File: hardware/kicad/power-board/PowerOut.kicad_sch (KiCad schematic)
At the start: 17 parts, among them J1 3.3V LoRaWAN, J2 3.3V SWARM, J3 Conn_01x02, J4 5V, J6 12V

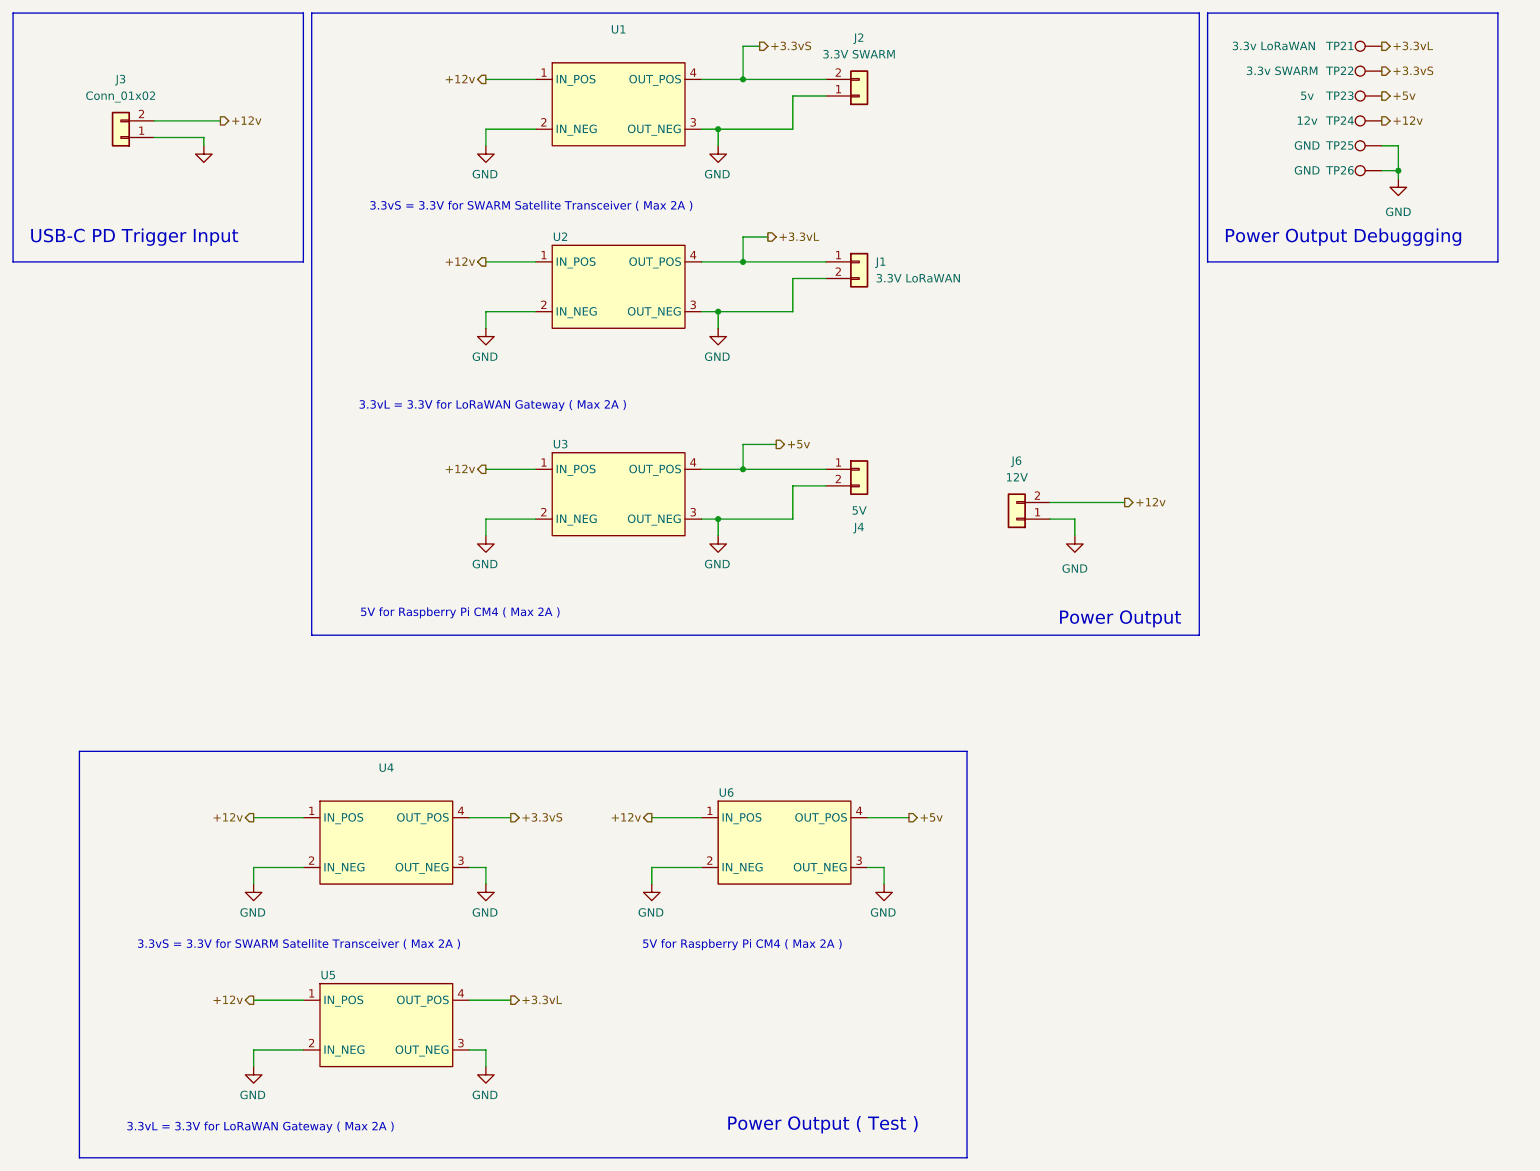
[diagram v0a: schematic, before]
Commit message: fix power polarity in power board test
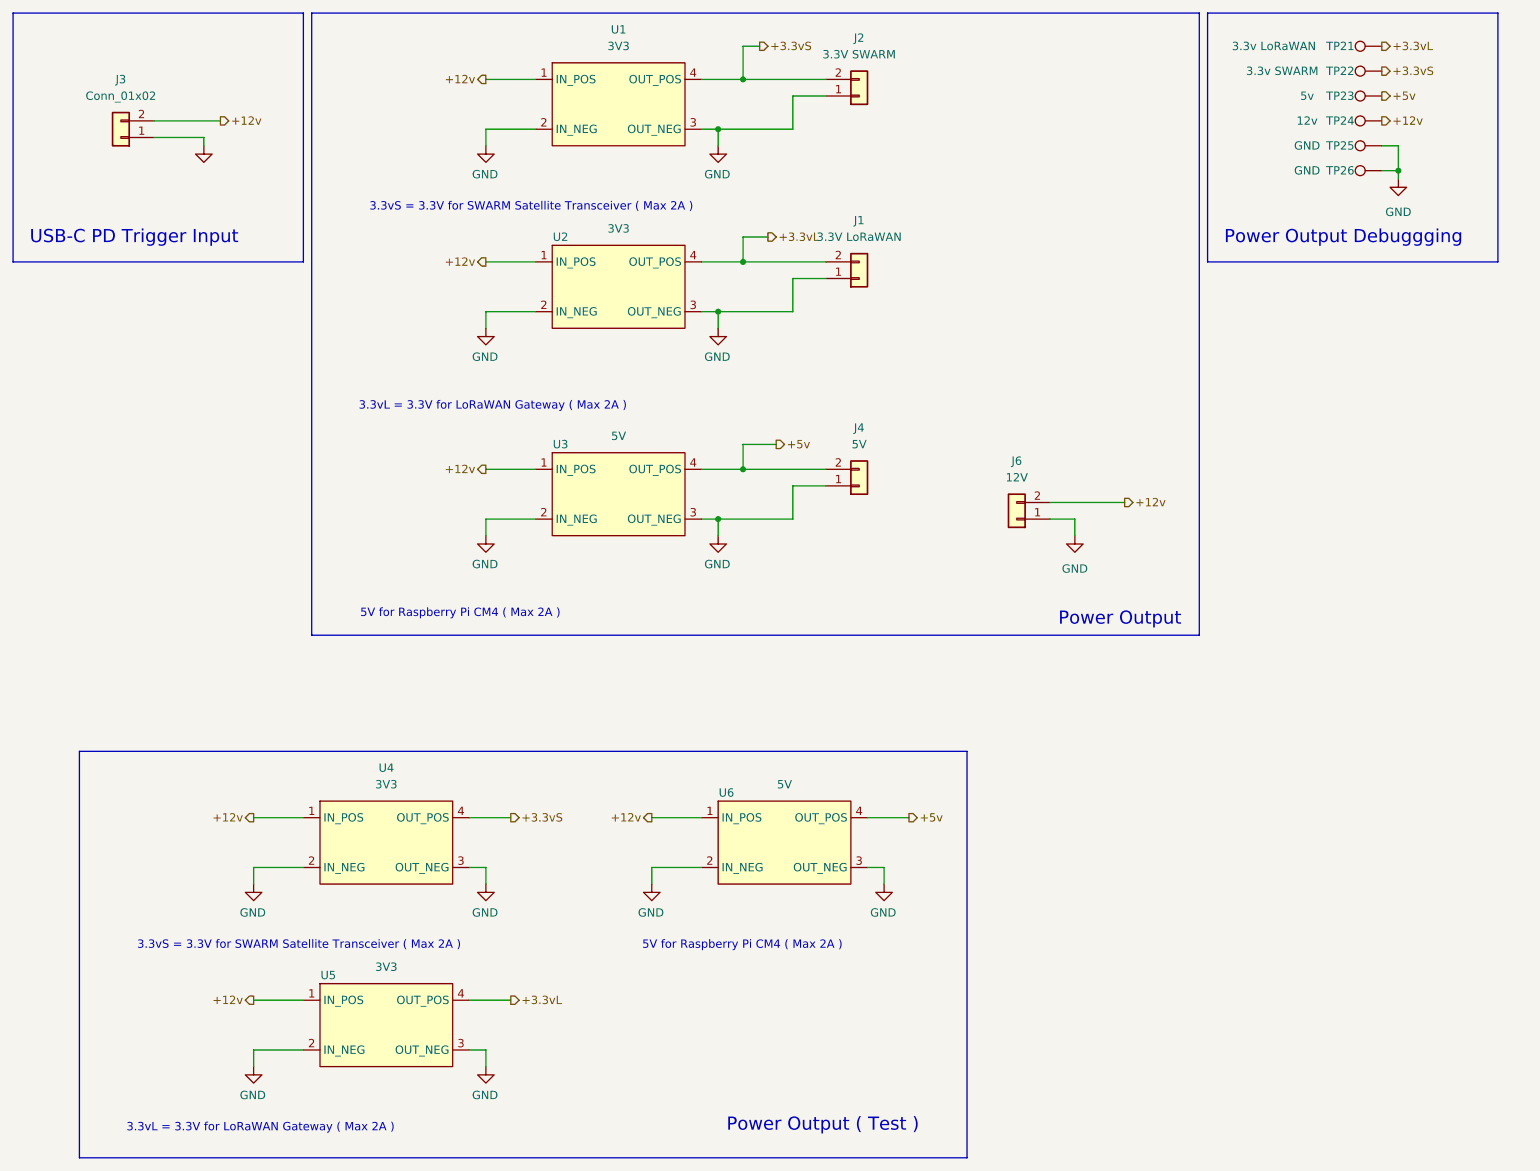
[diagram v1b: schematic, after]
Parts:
- U1, U2: value (none) -> 3V3; footprint (none) -> Teapot:LM2596Module
- U3: value (none) -> 5V; footprint (none) -> Teapot:LM2596Module
- U4, U5: value (none) -> 3V3; footprint (none) -> Teapot:MiniMP1584ENModule
- U6: value (none) -> 5V; footprint (none) -> Teapot:MiniMP1584ENModule
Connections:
- net +3.3vL: now also J1.2 (Pin_2); no longer J1.1 (Pin_1)
- net +5v: now also J4.2 (Pin_2); no longer J4.1 (Pin_1)
- net GND: now also J1.1 (Pin_1), J4.1 (Pin_1); no longer J1.2 (Pin_2), J4.2 (Pin_2)
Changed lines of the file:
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@@
     (pin "1")
   )
-  (symbol (lib_id "Connector_Generic:Conn_01x02") (at 144.78 85.09 0) (unit 1)
-    (in_bom yes) (on_board yes)
-    (property "Reference" "J4" (id 0) (at 144.78 93.98 0))
-    (property "Value" "5V" (id 1) (at 144.78 91.44 0))
-    (property "Footprint" "Connector_Wire:SolderWire-0.5sqmm_1x02_P4.8mm_D0.9mm_OD2.3mm" (id 2) (at 144.78 85.09 0)
-      (effects (font (size 1.27 1.27)) hide)
-    )
-    (property "Datasheet" "~" (id 3) (at 144.78 85.09 0)
+  (symbol (lib_id "Connector_Generic:Conn_01x02") (at 144.78 87.63 0) (mirror x) (unit 1)
+    (in_bom yes) (on_board yes)
+    (property "Reference" "J4" (id 0) (at 144.78 78.74 0))
+    (property "Value" "5V" (id 1) (at 144.78 81.28 0))
+    (property "Footprint" "Connector_Wire:SolderWire-0.5sqmm_1x02_P4.8mm_D0.9mm_OD2.3mm" (id 2) (at 144.78 87.63 0)
+      (effects (font (size 1.27 1.27)) hide)
+    )
+    (property "Datasheet" "~" (id 3) (at 144.78 87.63 0)
       (effects (font (size 1.27 1.27)) hide)
     )
@@
     (in_bom yes) (on_board yes)
     (property "Reference" "U6" (id 0) (at 124.46 134.62 0))
-    (property "Value" "" (id 1) (at 133.35 133.35 0))
-    (property "Footprint" "" (id 2) (at 133.35 133.985 0)
+    (property "Value" "5V" (id 1) (at 133.35 133.35 0))
+    (property "Footprint" "Teapot:MiniMP1584ENModule" (id 2) (at 133.35 133.985 0)
       (effects (font (size 1.27 1.27)) hide)
     )
@@
     (in_bom yes) (on_board yes) (fields_autoplaced)
     (property "Reference" "U1" (id 0) (at 107.95 17.78 0))
-    (property "Value" "" (id 1) (at 107.95 20.32 0))
-    (property "Footprint" "" (id 2) (at 107.95 20.955 0)
+    (property "Value" "3V3" (id 1) (at 107.95 20.32 0))
+    (property "Footprint" "Teapot:LM2596Module" (id 2) (at 107.95 20.955 0)
       (effects (font (size 1.27 1.27)) hide)
     )
@@
     (in_bom yes) (on_board yes) (fields_autoplaced)
     (property "Reference" "U4" (id 0) (at 72.39 130.81 0))
-    (property "Value" "" (id 1) (at 72.39 133.35 0))
-    (property "Footprint" "" (id 2) (at 72.39 133.985 0)
+    (property "Value" "3V3" (id 1) (at 72.39 133.35 0))
+    (property "Footprint" "Teapot:MiniMP1584ENModule" (id 2) (at 72.39 133.985 0)
       (effects (font (size 1.27 1.27)) hide)
     )
@@
     (pin "1")
   )
-  (symbol (lib_id "Connector_Generic:Conn_01x02") (at 144.78 53.34 0) (unit 1)
-    (in_bom yes) (on_board yes) (fields_autoplaced)
-    (property "Reference" "J1" (id 0) (at 147.32 53.3399 0)
-      (effects (font (size 1.27 1.27)) (justify left))
-    )
-    (property "Value" "3.3V LoRaWAN" (id 1) (at 147.32 55.8799 0)
-      (effects (font (size 1.27 1.27)) (justify left))
-    )
-    (property "Footprint" "Connector_Wire:SolderWire-0.5sqmm_1x02_P4.8mm_D0.9mm_OD2.3mm" (id 2) (at 144.78 53.34 0)
-      (effects (font (size 1.27 1.27)) hide)
-    )
-    (property "Datasheet" "~" (id 3) (at 144.78 53.34 0)
+  (symbol (lib_id "Connector_Generic:Conn_01x02") (at 144.78 55.88 0) (mirror x) (unit 1)
+    (in_bom yes) (on_board yes) (fields_autoplaced)
+    (property "Reference" "J1" (id 0) (at 144.78 46.99 0))
+    (property "Value" "3.3V LoRaWAN" (id 1) (at 144.78 49.53 0))
+    (property "Footprint" "Connector_Wire:SolderWire-0.5sqmm_1x02_P4.8mm_D0.9mm_OD2.3mm" (id 2) (at 144.78 55.88 0)
+      (effects (font (size 1.27 1.27)) hide)
+    )
+    (property "Datasheet" "~" (id 3) (at 144.78 55.88 0)
       (effects (font (size 1.27 1.27)) hide)
     )
@@
     (in_bom yes) (on_board yes)
     (property "Reference" "U2" (id 0) (at 99.06 49.53 0))
-    (property "Value" "" (id 1) (at 107.95 48.26 0))
-    (property "Footprint" "" (id 2) (at 107.95 48.895 0)
+    (property "Value" "3V3" (id 1) (at 107.95 48.26 0))
+    (property "Footprint" "Teapot:LM2596Module" (id 2) (at 107.95 48.895 0)
       (effects (font (size 1.27 1.27)) hide)
     )
@@
     (in_bom yes) (on_board yes)
     (property "Reference" "U3" (id 0) (at 99.06 81.28 0))
-    (property "Value" "" (id 1) (at 107.95 80.01 0))
-    (property "Footprint" "" (id 2) (at 107.95 80.645 0)
+    (property "Value" "5V" (id 1) (at 107.95 80.01 0))
+    (property "Footprint" "Teapot:LM2596Module" (id 2) (at 107.95 80.645 0)
       (effects (font (size 1.27 1.27)) hide)
     )
@@
     (in_bom yes) (on_board yes)
     (property "Reference" "U5" (id 0) (at 63.5 162.56 0))
-    (property "Value" "" (id 1) (at 72.39 161.29 0))
-    (property "Footprint" "" (id 2) (at 72.39 161.925 0)
-      (effects (font (size 1.27 1.27)) hide)
-    )
+    (property "Value" "3V3" (id 1) (at 72.39 161.29 0))
+    (property "Footprint" "Teapot:MiniMP1584ENModule" (id 2) (at 72.39 161.925 0)
+      (effects (font (size 1.27 1.27)) hide)
+    )
